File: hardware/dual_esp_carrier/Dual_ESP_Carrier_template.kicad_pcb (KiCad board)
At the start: 2 copper layers, 100 x 100 mm, 23 parts, among them J1 ESP32_T_LANDSCAPE, J2 ESP32_B_LANDSCAPE, J3 SX1278_LORA_2x4, J6 GPS_LC29H_7PIN, SW1 subir ancora, SW2 MODE, SW3 largar ancora, SW4 BOOT

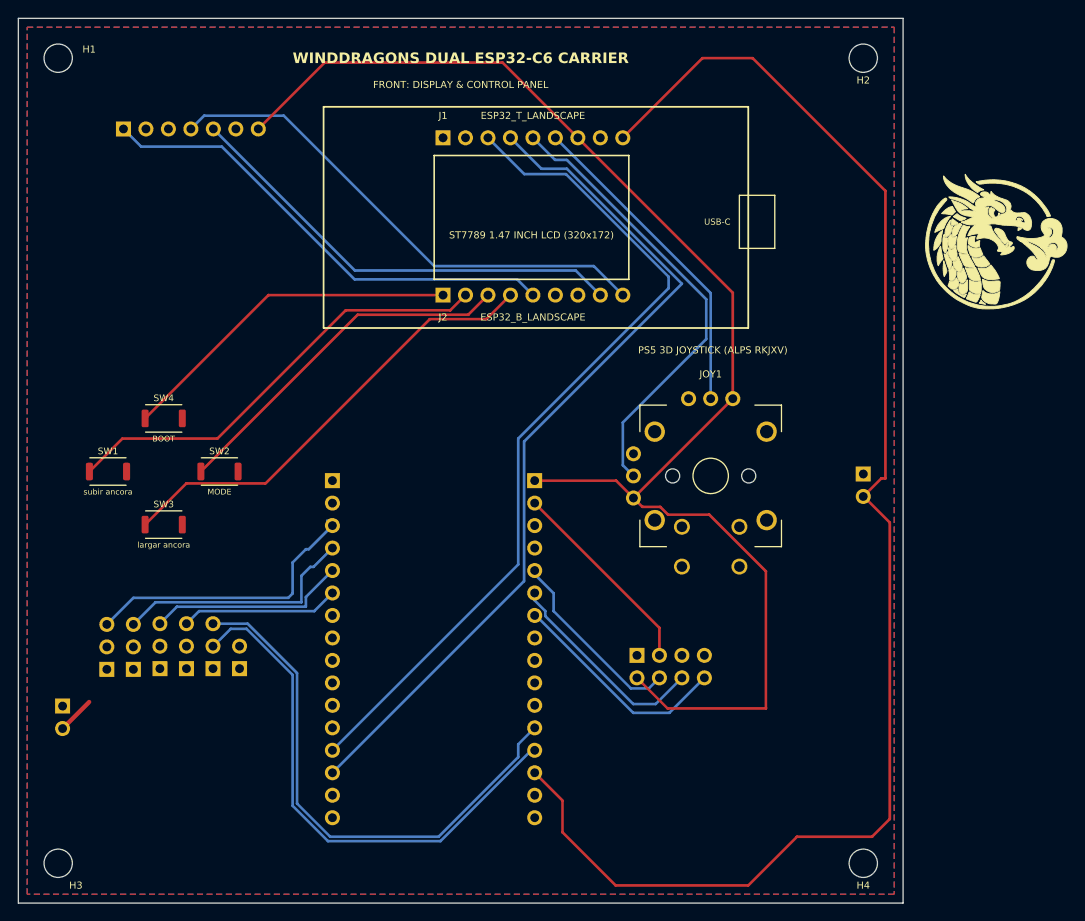
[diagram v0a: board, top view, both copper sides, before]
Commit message: feat: update dual ESP carrier PCB layout and add power and UART test sources
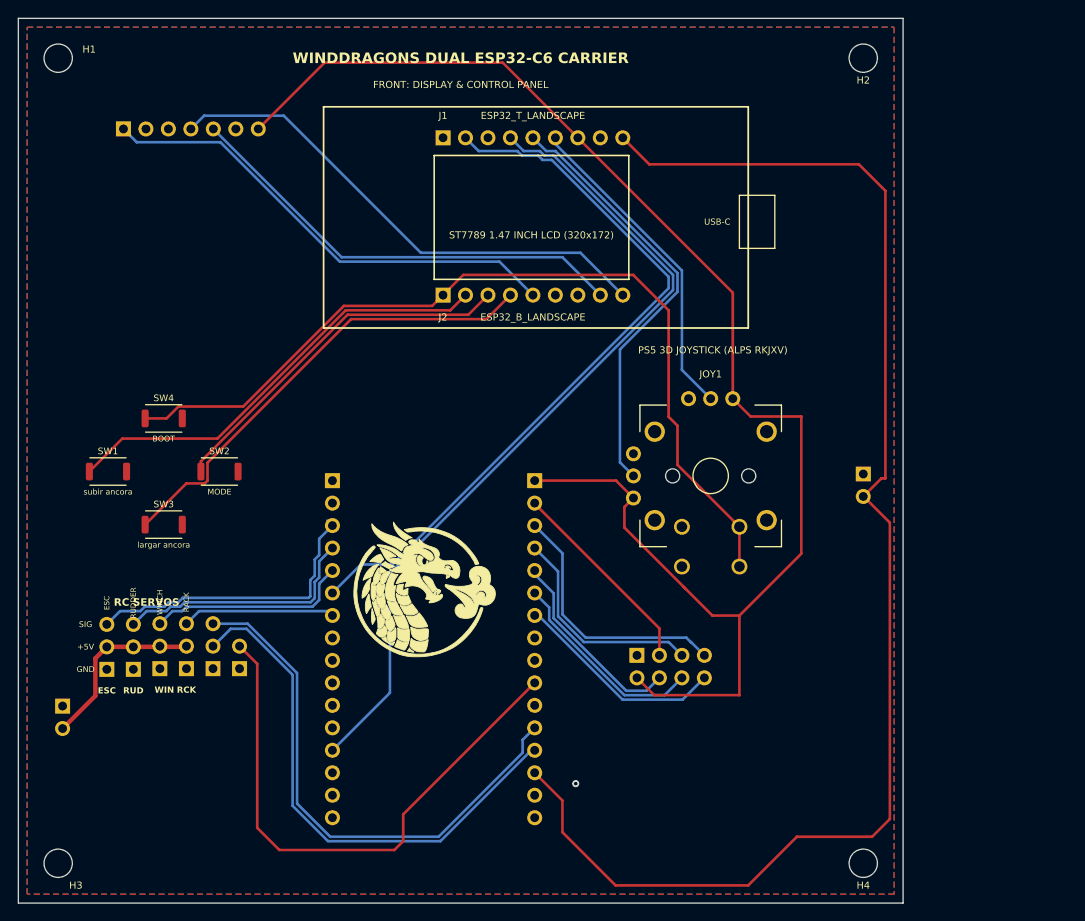
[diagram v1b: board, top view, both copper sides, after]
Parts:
- ESC: value ESC (IO4) -> ESC; moved to F.Cu
- RCK: value RACK (IO7) -> RACK; moved to F.Cu
- RUD: value RUDDER (IO5) -> RUDDER; moved to F.Cu
- WIN: value WINCH (IO6) -> WINCH; moved to F.Cu
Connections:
- J1 pad 2: /IO4_FREE -> /INTER_TX_M2S
- J1 pad 3: /INTER_TX_M2S -> /IO3_FREE
- J_DK_R pad 13: /INTER_TX_M2S -> /INTER_RX_S2M
- J_DK_R pad 14: /INTER_RX_S2M -> (no net)
- J_DK_R pad 6: /SERVO_RACK -> /INTER_TX_M2S
- J_DK_R pad 7: (no net) -> /SERVO_RACK
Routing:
- net /WATER_SENS: track 0.00 -> 63.4 mm
- net /IO9_BOOT: track 39.4 -> 99.8 mm
- net /LORA_MISO: track 0.00 -> 29.3 mm
- net /LORA_SCK: track 0.00 -> 24.6 mm
- net /+5V_SERVO: track 4.36 -> 20.3 mm
- net /INTER_TX_M2S: track 96.2 -> 83.0 mm
- net /+3V3: track 157.3 -> 168.0 mm
- net /+5V: track 163.8 -> 156.4 mm
- net /INTER_RX_S2M: track 97.8 -> 94.5 mm
- net /JOY_Y: track 51.5 -> 48.9 mm
- net /LORA_DIO0: track 25.4 -> 24.1 mm
- net /IO20_DN: track 52.0 -> 53.2 mm
- net /SERVO_ESC: track 33.0 -> 34.2 mm
- net /LORA_MOSI: track 23.9 -> 23.1 mm
- net /LORA_NSS: track 21.6 -> 22.2 mm
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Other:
- board text added: "+5V"
- board text added: "GND"
- board text added: "RC SERVOS"
- board text added: "SIG"

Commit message: feat: add limit switch and strobe LED support to hardware and firmware
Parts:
- added J_LIMIT: LIMIT/ANC, Connector_PinHeader_2.54mm:PinHeader_1x02_P2.54mm_Vertical, F.Cu at (4.00, 73.6)
- added STRB: WS2812B, Connector_PinHeader_2.54mm:PinHeader_1x03_P2.54mm_Vertical, F.Cu at (7.00, 73.6)
- J1: value ESP32_T_LANDSCAPE -> ESP32_lafvin
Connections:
- J1 pad 2: /INTER_TX_M2S -> /IO4_FREE
- J1 pad 3: /IO3_FREE -> /JOY_X
- J1 pad 4: /INTER_RX_S2M -> /INTER_TX_M2S
- J1 pad 5: /JOY_Y -> /INTER_RX_S2M
- J1 pad 6: /JOY_X -> /JOY_Y
- J6 pad 4: /GPS_TX -> /GPS_RX
- J6 pad 5: /GPS_RX -> /GPS_TX
- J_DK_R pad 10: (no net) -> /ANCHOR_LIMIT
- J_DK_R pad 9: (no net) -> /STROBE_DIN
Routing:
- net /ANCHOR_LIMIT: track 0.00 -> 46.7 mm, vias 0 -> 1
- net /STROBE_DIN: track 0.00 -> 42.6 mm
- net /JOY_X: track 36.8 -> 53.7 mm
- net /GPS_PPS: track 54.1 -> 63.1 mm
- net /GPS_RX: track 51.5 -> 58.2 mm
- net /INTER_RX_S2M: track 94.5 -> 99.6 mm
- net /JOY_Y: track 48.9 -> 53.6 mm
- net /+3V3: track 168.0 -> 164.6 mm
- net /+5V_SERVO: track 20.3 -> 23.3 mm
- net /INTER_TX_M2S: track 83.0 -> 85.6 mm
- net /GPS_TX: track 57.8 -> 58.5 mm
- net /GND: vias 1 -> 0
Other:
- board text added: "WINDDRAGONS VIRTUAL REGATTA SYSTEM V1.0"
- board text removed: "WINDDRAGONS DUAL ESP32-C6 CARRIER"

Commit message: feat: separate 3.3V power domains for Lafvin and DevKitC C6 on carrier board
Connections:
- J3 pad 2: /+3V3 -> /+3V3_C6
- J_DK_L pad 1: /+3V3 -> /+3V3_C6
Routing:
- net /+3V3_C6: track 0.00 -> 52.6 mm
- net /+3V3: track 164.6 -> 128.2 mm, vias 0 -> 1
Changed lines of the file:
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@@
 			(layers "*.Cu" "*.Mask" "B.SilkS")
 			(remove_unused_layers no)
-			(net "/+3V3")
+			(net "/+3V3_C6")
 		)
 		(pad "3" thru_hole circle
@@
 			(layers "*.Cu" "*.Mask" "B.SilkS")
 			(remove_unused_layers no)
-			(net "/+3V3")
+			(net "/+3V3_C6")
 		)
 		(pad "2" thru_hole circle
@@
 	)
 	(segment
-		(start 87 46)
-		(end 85.5 44.5)
+		(start 87 62)
+		(end 87 60.5)
 		(width 0.3)
 		(layer "F.Cu")
@@
 	)
 	(segment
-		(start 75.222366 64.277634)
-		(end 75.444733 64.5)
+		(start 87 46)
+		(end 85.5 44.5)
 		(width 0.3)
 		(layer "F.Cu")
@@
 	)
 	(segment
-		(start 69.5225 54.215)
-		(end 68.5 55.2375)
-		(width 0.3)
-		(layer "F.Cu")
-		(net "/+3V3")
-	)
-	(segment
-		(start 72.38 77)
-		(end 79 77)
-		(width 0.3)
-		(layer "F.Cu")
-		(net "/+3V3")
-	)
-	(segment
 		(start 63.24 13.5)
 		(end 54.74 5)
@@
 	)
 	(segment
-		(start 68.5 55.2375)
-		(end 68.5 57.555268)
-		(width 0.3)
-		(layer "F.Cu")
-		(net "/+3V3")
-	)
-	(segment
 		(start 80.7525 31.0125)
 		(end 63.24 13.5)
@@
 	)
 	(segment
-		(start 81.5 67.5)
-		(end 78.444732 67.5)
-		(width 0.3)
-		(layer "F.Cu")
-		(net "/+3V3")
-	)
-	(segment
-		(start 58.36 52.25)
-		(end 67.5575 52.25)
-		(width 0.3)
-		(layer "F.Cu")
-		(net "/+3V3")
-	)
-	(segment
-		(start 81.5 67.5)
-		(end 87 62)
-		(width 0.3)
-		(layer "F.Cu")
-		(net "/+3V3")
-	)
-	(segment
 		(start 80.7525 42.985)
 		(end 80.7525 31.0125)
@@
 	)
 	(segment
-		(start 80 72.5)
-		(end 81.5 71)
-		(width 0.3)
-		(layer "F.Cu")
-		(net "/+3V3")
-	)
-	(segment
 		(start 87 62)
 		(end 87 46)
@@
 	)
 	(segment
-		(start 80 76)
-		(end 80 72.5)
-		(width 0.3)
-		(layer "F.Cu")
-		(net "/+3V3")
-	)
-	(segment
-		(start 79 77)
-		(end 80 76)
-		(width 0.3)
-		(layer "F.Cu")
-		(net "/+3V3")
-	)
-	(segment
-		(start 68.5 57.555268)
-		(end 75.222366 64.277634)
-		(width 0.3)
-		(layer "F.Cu")
-		(net "/+3V3")
-	)
-	(segment
-		(start 81.5 71)
-		(end 81.5 67.5)
-		(width 0.3)
-		(layer "F.Cu")
-		(net "/+3V3")
-	)
-	(segment
 		(start 54.74 5)
 		(end 34.62 5)
@@
 	)
 	(segment
-		(start 67.5575 52.25)
-		(end 69.5225 54.215)
+		(start 34.62 5)
+		(end 27.12 12.5)
 		(width 0.3)
 		(layer "F.Cu")
 		(net "/+3V3")
 	)
-	(segment
-		(start 69.92 74.54)
-		(end 72.38 77)
-		(width 0.3)
-		(layer "F.Cu")
+	(via
+		(at 87 60.5)
+		(size 0.8)
+		(drill 0.4)
+		(layers "F.Cu" "B.Cu")
+		(free yes)
 		(net "/+3V3")
 	)
 	(segment
-		(start 34.62 5)
-		(end 27.12 12.5)
+		(start 87 60.5)
+		(end 69.5225 60.5)
 		(width 0.3)
-		(layer "F.Cu")
+		(layer "B.Cu")
 		(net "/+3V3")
 	)
 	(segment
-		(start 78.444732 67.5)
-		(end 75.222366 64.277634)
+		(start 69.5225 60.5)
+		(end 69.5225 54.215)
 		(width 0.3)
-		(layer "F.Cu")
+		(layer "B.Cu")
 		(net "/+3V3")
 	)
@@
 	)
 	(segment
+		(start 72.38 77)
+		(end 79 77)
+		(width 0.3)
+		(layer "F.Cu")
+		(net "/+3V3_C6")
+	)
+	(segment
+		(start 81.5 67.5)
+		(end 78.444732 67.5)
+		(width 0.3)
+		(layer "F.Cu")
+		(net "/+3V3_C6")
+	)
+	(segment
+		(start 58.36 52.25)
+		(end 66.5 52.25)
+		(width 0.3)
+		(layer "F.Cu")
+		(net "/+3V3_C6")
+	)
+	(segment
+		(start 80 72.5)
+		(end 81.5 71)
+		(width 0.3)
+		(layer "F.Cu")
+		(net "/+3V3_C6")
+	)
+	(segment
+		(start 80 76)
+		(end 80 72.5)
+		(width 0.3)
+		(layer "F.Cu")
+		(net "/+3V3_C6")
+	)
+	(segment
+		(start 79 77)
+		(end 80 76)
+		(width 0.3)
+		(layer "F.Cu")
+		(net "/+3V3_C6")
+	)
+	(segment
+		(start 68.5 57.555268)
+		(end 75.222366 64.277634)
+		(width 0.3)
+		(layer "F.Cu")
+		(net "/+3V3_C6")
+	)
+	(segment
+		(start 81.5 71)
+		(end 81.5 67.5)
+		(width 0.3)
+		(layer "F.Cu")
+		(net "/+3V3_C6")
+	)
+	(segment
+		(start 69.92 74.54)
+		(end 72.38 77)
+		(width 0.3)
+		(layer "F.Cu")
+		(net "/+3V3_C6")
+	)
+	(segment
+		(start 78.444732 67.5)
+		(end 75.222366 64.277634)
+		(width 0.3)
+		(layer "F.Cu")
+		(net "/+3V3_C6")
+	)
+	(segment
 		(start 72.46 68.96)
 		(end 58.36 54.86)
@@
 		(net "/BATT_CURR")
 	)
+	(segment
+		(start 66.5 52.25)
+		(end 66.5 56.5)
+		(width 0.3)
+		(layer "F.Cu")
+		(net "/+3V3_C6")
+	)
+	(segment
+		(start 66.5 56.5)
+		(end 67.56 57.56)
+		(width 0.3)
+		(layer "F.Cu")
+		(net "/+3V3_C6")
+	)
+	(segment
+		(start 67.56 57.56)
+		(end 68.5 57.56)
+		(width 0.3)
+		(layer "F.Cu")
+		(net "/+3V3_C6")
+	)
 	(zone

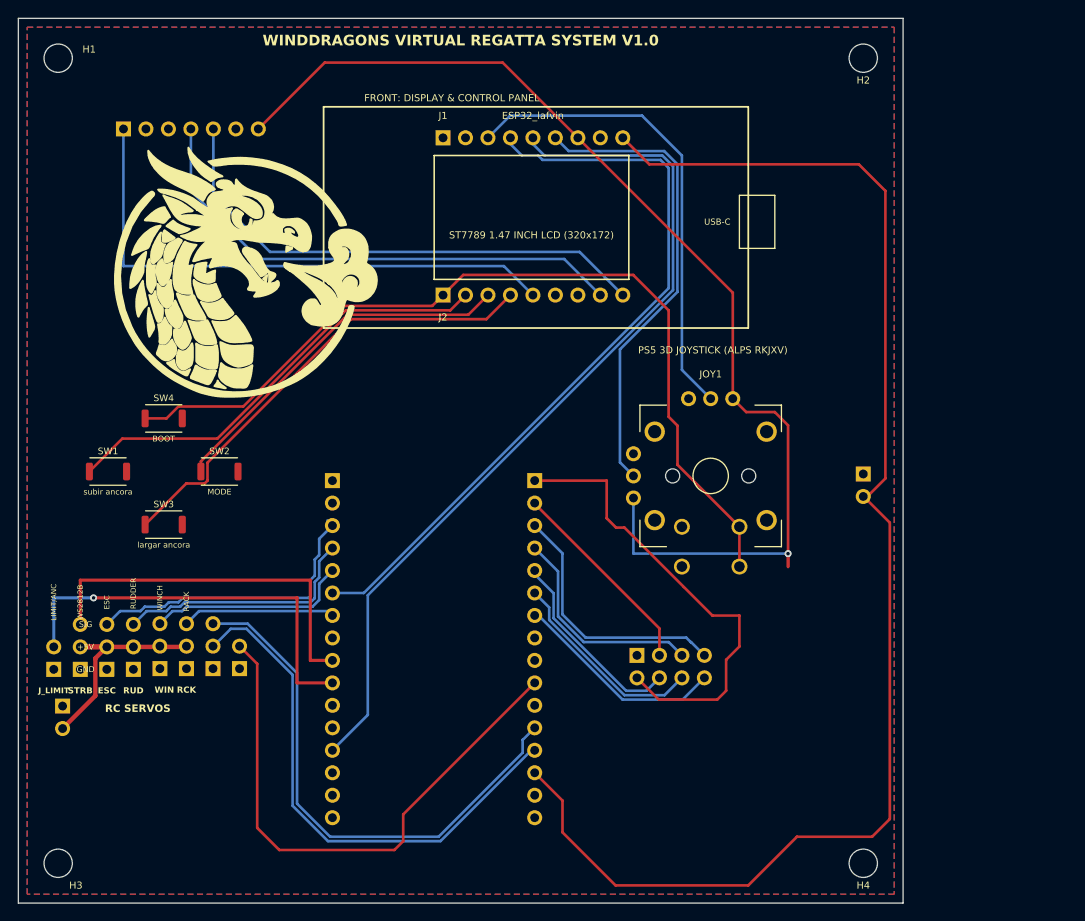
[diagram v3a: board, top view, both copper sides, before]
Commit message: feat: update Dual ESP carrier PCB layout, gerbers, and pinout documentation
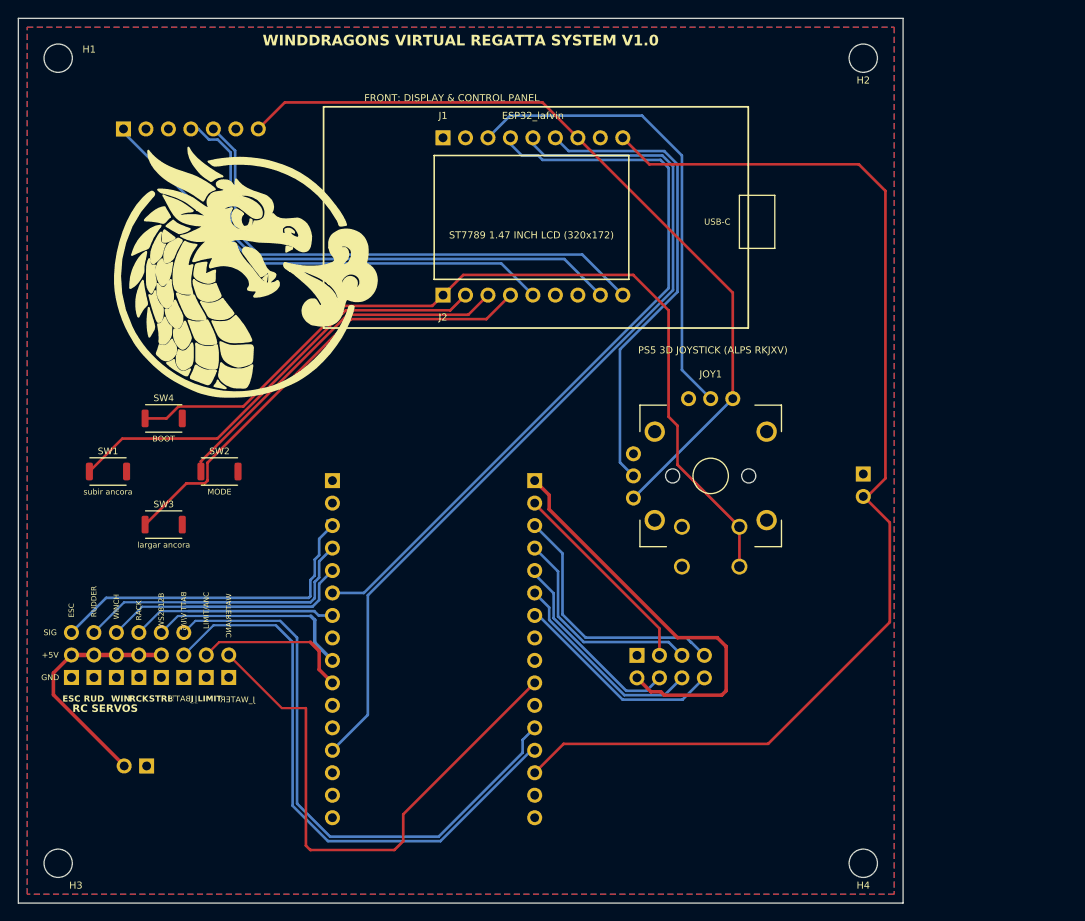
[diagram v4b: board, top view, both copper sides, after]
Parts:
- J_BATT, J_WATER: moved to F.Cu
- moved J_LIMIT 17.3 mm to (21.2, 74.5)
- moved J_PWR_SRV 11.7 mm to (14.5, 84.5), turned to -90 degrees
- moved STRB 9.21 mm to (16.2, 74.5)
- moved RCK 5.47 mm to (13.6, 74.5)
- moved WIN 5.02 mm to (11.1, 74.5)
- moved RUD 4.55 mm to (8.54, 74.5)
- moved ESC 4.10 mm to (6.00, 74.5)
- moved J_BATT 3.45 mm to (18.7, 74.5)
- moved J_WATER 1.58 mm to (23.8, 74.5)
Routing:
- net /+3V3: track 128.2 -> 91.6 mm, vias 1 -> 0
- net /ANCHOR_LIMIT: track 46.7 -> 18.0 mm, vias 1 -> 0
- net /+5V: track 156.4 -> 130.7 mm
- net /STROBE_DIN: track 42.6 -> 23.7 mm
- net /GPS_PPS: track 63.1 -> 54.3 mm
- net /SERVO_RACK: track 17.3 -> 23.8 mm
- net /BATT_VOLT: track 60.9 -> 67.2 mm
- net /BATT_CURR: track 60.0 -> 66.2 mm
- net /+3V3_C6: track 52.6 -> 46.4 mm
- net /SERVO_WINCH: track 23.1 -> 28.4 mm
- net /SERVO_RUDDER: track 28.2 -> 33.1 mm
- net /SERVO_ESC: track 34.2 -> 38.5 mm
- net /+5V_SERVO: track 23.3 -> 26.9 mm
- net /GPS_RX: track 58.2 -> 59.4 mm
- net /WATER_SENS: track 63.4 -> 62.4 mm
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
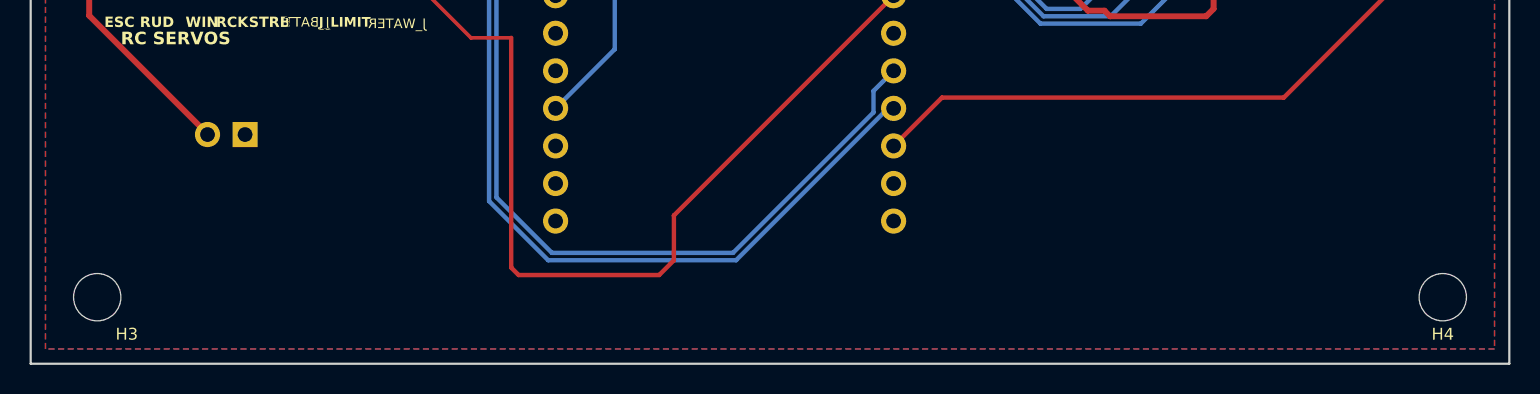
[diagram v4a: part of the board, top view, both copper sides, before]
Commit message: feat: add Hall sensor footprint and mounting holes to dual ESP carrier PCB
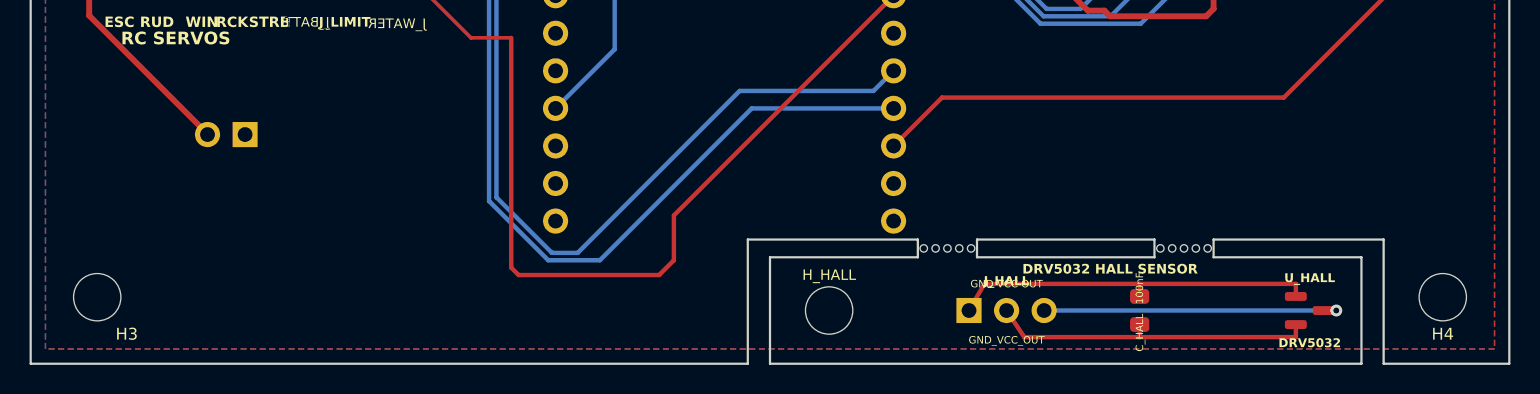
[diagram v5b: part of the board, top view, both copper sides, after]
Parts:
- added C_HALL: 100nF, Capacitor_SMD:C_0805_2012Metric, F.Cu at (75.0, 96.4)
- added H_HALL: M3_MOUNT, MountingHole:MountingHole_3.2mm_M3, F.Cu at (54.0, 96.4)
- added J_HALL: GND_VCC_OUT, Connector_PinHeader_2.54mm:PinHeader_1x03_P2.54mm_Horizontal, F.Cu at (66.0, 96.4)
- added STAMP: , MountingHole:MountingHole_0.5mm, F.Cu at (76.4, 92.2)
- added STAMP: , MountingHole:MountingHole_0.5mm, F.Cu at (62.0, 92.2)
- added STAMP: , MountingHole:MountingHole_0.5mm, F.Cu at (62.8, 92.2)
- added STAMP: , MountingHole:MountingHole_0.5mm, F.Cu at (79.6, 92.2)
- added STAMP: , MountingHole:MountingHole_0.5mm, F.Cu at (77.2, 92.2)
- added STAMP: , MountingHole:MountingHole_0.5mm, F.Cu at (63.6, 92.2)
- added STAMP: , MountingHole:MountingHole_0.5mm, F.Cu at (78.8, 92.2)
- added STAMP: , MountingHole:MountingHole_0.5mm, F.Cu at (61.2, 92.2)
- added STAMP: , MountingHole:MountingHole_0.5mm, F.Cu at (60.4, 92.2)
- added STAMP: , MountingHole:MountingHole_0.5mm, F.Cu at (78.0, 92.2)
- added U_HALL: DRV5032, Package_TO_SOT_SMD:SOT-23, F.Cu at (86.5, 96.4)
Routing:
- net /HALL_GND: track 0.00 -> 24.8 mm
- net /HALL_VCC: track 0.00 -> 22.2 mm
- net /HALL_OUT: track 0.00 -> 20.6 mm, vias 0 -> 1
- net /BATT_VOLT: track 67.2 -> 66.4 mm
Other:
- outline, holes or cut-outs redrawn
- board text added: "DRV5032 HALL SENSOR"
- board text added: "GND VCC OUT"
- board text added: "WINCH SPOOL"

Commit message: update Dual_ESP_Carrier hardware files and pinout documentation for the anchor Hall sensor connector
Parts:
- added HALL: ANCHOR HALL, Connector_PinHeader_2.54mm:PinHeader_1x03_P2.54mm_Vertical, F.Cu at (26.3, 74.5)
- J_BATT: value BATT V/I/G -> BATT CUR/VOLT
- J_LIMIT: value LIMIT/ANC -> ANCHOR SENSOR
- J_PWR_SRV: value 5V_SERVO -> 5V | 6V SBEC
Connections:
- J_DK_R pad 8: (no net) -> /ANCHOR_HALL
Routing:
- net /+3V3_C6: track 46.4 -> 86.7 mm
- net /ANCHOR_HALL: track 0.00 -> 9.43 mm
- net /WATER_SENS: track 62.4 -> 64.3 mm
- net /BATT_CURR: track 66.2 -> 67.3 mm
- net /ANCHOR_LIMIT: track 18.0 -> 17.5 mm, vias 0 -> 1
